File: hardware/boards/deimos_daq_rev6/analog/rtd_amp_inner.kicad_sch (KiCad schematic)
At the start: 22 parts, among them IC4001 INA826AIDR, IC4002 TLV333IDBVR, IC4003 TLV333IDBVR, U4001 NTJD4001NT1G

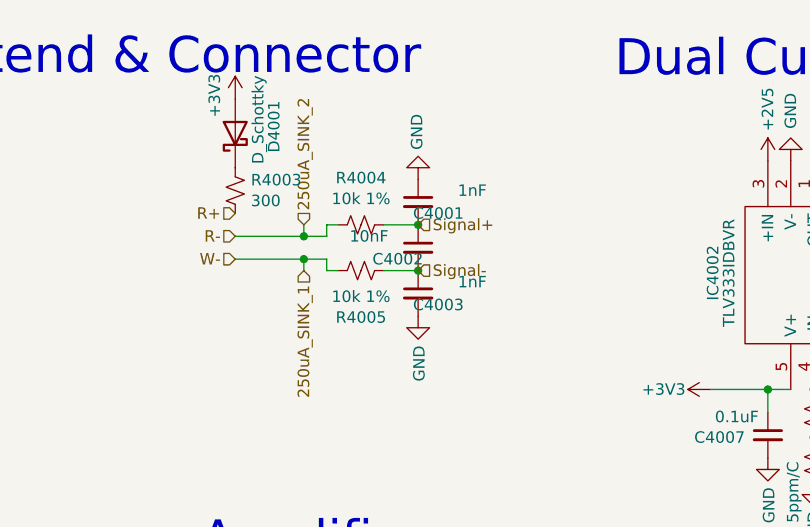
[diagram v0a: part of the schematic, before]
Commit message: move ovp diodes behind filter amps. wip to implement 5V LDO.
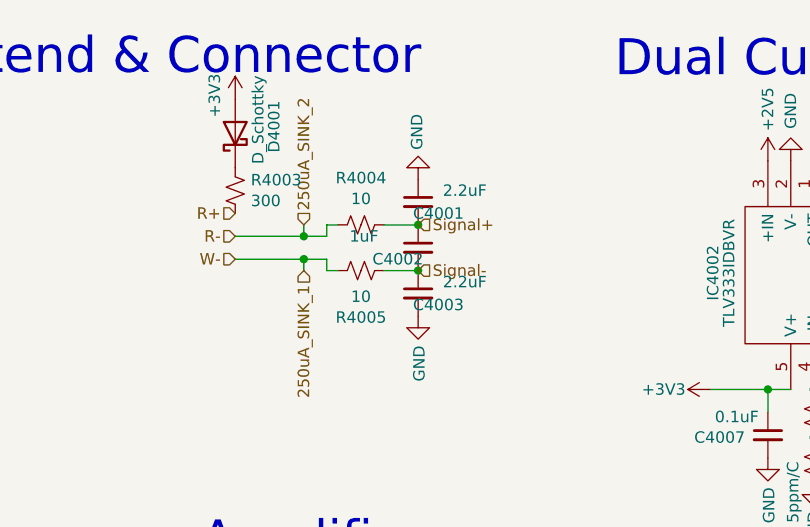
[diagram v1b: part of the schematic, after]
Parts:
- C4001, C4003: value 1nF -> 2.2uF
- C4002: value 10nF -> 1uF
- R4004, R4005: value 10k 1% -> 10
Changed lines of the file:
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@@
 			)
 		)
-		(property "Value" "10k 1%"
+		(property "Value" "10"
 			(at 121.92 65.4304 90)
 			(effects
@@
 			)
 		)
-		(property "Value" "1nF"
+		(property "Value" "2.2uF"
 			(at 135.89 64.516 0)
 			(effects
@@
 			)
 		)
-		(property "Value" "10nF"
+		(property "Value" "1uF"
 			(at 120.65 69.596 0)
 			(effects
@@
 			)
 		)
-		(property "Value" "10k 1%"
+		(property "Value" "10"
 			(at 121.92 76.3016 90)
 			(effects
@@
 			)
 		)
-		(property "Value" "1nF"
+		(property "Value" "2.2uF"
 			(at 135.89 74.676 0)
 			(effects

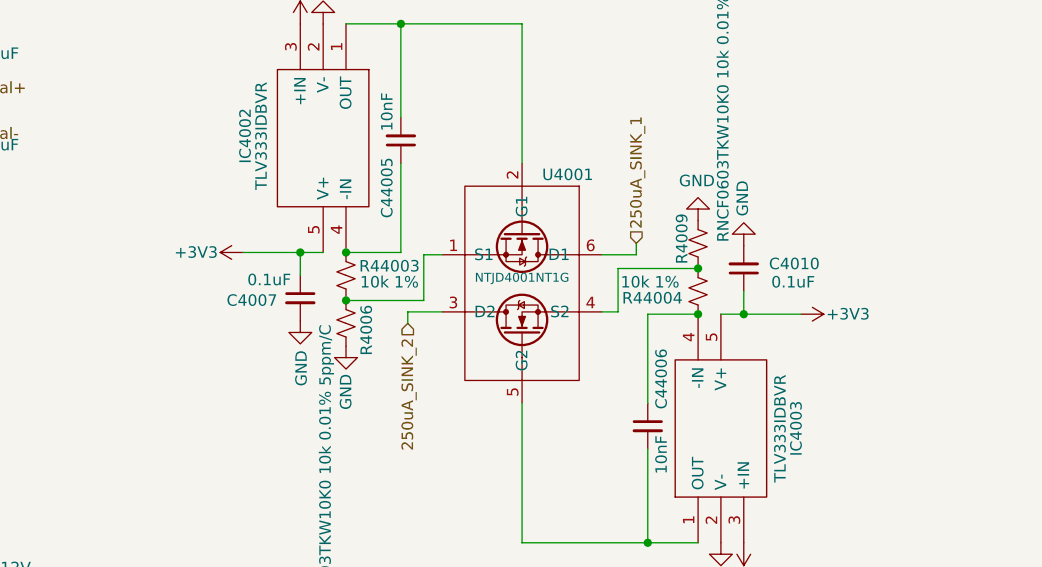
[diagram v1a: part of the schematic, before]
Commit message: run rtd amp current sinks on 5V supply
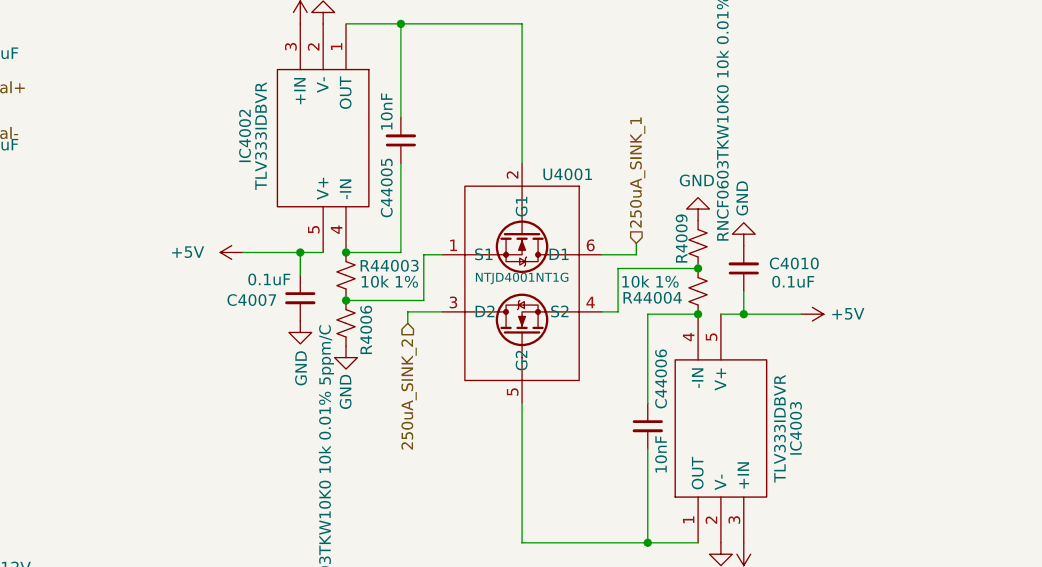
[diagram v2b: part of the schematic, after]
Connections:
- net +3V3: no longer C4007.1, C4010.1, IC4002.5 (V+), IC4003.5 (V+)
- new net +5V: C4007.1, C4010.1, IC4002.5 (V+), IC4003.5 (V+)
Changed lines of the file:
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@@
-	)
-	(symbol
-		(lib_id "power:+3V3")
-		(at 222.758 93.472 270)
-		(unit 1)
-		(exclude_from_sim no)
-		(in_bom yes)
-		(on_board yes)
-		(dnp no)
-		(property "Reference" "#PWR126"
-			(at 218.948 93.472 0)
-			(effects
-				(font
-					(size 1.27 1.27)
-				)
-				(hide yes)
-			)
-		)
-		(property "Value" "+3V3"
-			(at 225.552 93.472 90)
-			(effects
-				(font
-					(size 1.27 1.27)
-				)
-				(justify left)
-			)
-		)
-		(property "Footprint" ""
-			(at 222.758 93.472 0)
-			(effects
-				(font
-					(size 1.27 1.27)
-				)
-				(hide yes)
-			)
-		)
-		(property "Datasheet" ""
-			(at 222.758 93.472 0)
-			(effects
-				(font
-					(size 1.27 1.27)
-				)
-				(hide yes)
-			)
-		)
-		(property "Description" "Power symbol creates a global label with name \"+3V3\""
-			(at 222.758 93.472 0)
-			(effects
-				(font
-					(size 1.27 1.27)
-				)
-				(hide yes)
-			)
-		)
-		(pin "1"
-		)
-		(instances
-			(project "analog_i"
-				(path "/5a60c4b1-b6cb-416e-8883-8291fa089b87/c2baf18d-2b19-4edb-98b3-535275ee271f/a9caaa1d-d23d-426e-af7e-b0ee1cb64b05"
-					(reference "#PWR126")
-					(unit 1)
-				)
-				(path "/5a60c4b1-b6cb-416e-8883-8291fa089b87/c2baf18d-2b19-4edb-98b3-535275ee271f/19141585-7846-417a-91df-f61215fe3233/76bdcc3c-aeb3-45bb-bfec-f68418164bd8"
-					(reference "#PWR174")
-					(unit 1)
-				)
-				(path "/5a60c4b1-b6cb-416e-8883-8291fa089b87/c2baf18d-2b19-4edb-98b3-535275ee271f/1fbd3e63-3701-4f31-b722-16e65c25cea8/76bdcc3c-aeb3-45bb-bfec-f68418164bd8"
-					(reference "#PWR182")
-					(unit 1)
-				)
-				(path "/5a60c4b1-b6cb-416e-8883-8291fa089b87/c2baf18d-2b19-4edb-98b3-535275ee271f/fb5bb440-61c9-4bd3-9ab6-a463ad90c8bb/76bdcc3c-aeb3-45bb-bfec-f68418164bd8"
-					(reference "#PWR135")
-					(unit 1)
-				)
-			)
-			(project "analog_frontend_panel"
-				(path "/c241d083-1323-4b4a-a540-956d0afb7b72/a9caaa1d-d23d-426e-af7e-b0ee1cb64b05"
-					(reference "#PWR45003")
-					(unit 1)
-				)
-				(path "/c241d083-1323-4b4a-a540-956d0afb7b72/19141585-7846-417a-91df-f61215fe3233/76bdcc3c-aeb3-45bb-bfec-f68418164bd8"
-					(reference "#PWR46003")
-					(unit 1)
-				)
-				(path "/c241d083-1323-4b4a-a540-956d0afb7b72/1fbd3e63-3701-4f31-b722-16e65c25cea8/76bdcc3c-aeb3-45bb-bfec-f68418164bd8"
-					(reference "#PWR47003")
-					(unit 1)
-				)
-				(path "/c241d083-1323-4b4a-a540-956d0afb7b72/fb5bb440-61c9-4bd3-9ab6-a463ad90c8bb/76bdcc3c-aeb3-45bb-bfec-f68418164bd8"
-					(reference "#PWR44003")
-					(unit 1)
-				)
-			)
-		)
 	)
 	(symbol
@@
 	)
 	(symbol
-		(lib_id "power:+3V3")
+		(lib_id "power:+5V")
 		(at 160.782 86.614 90)
 		(unit 1)
@@
 		(on_board yes)
 		(dnp no)
-		(property "Reference" "#PWR125"
+		(fields_autoplaced yes)
+		(property "Reference" "#PWR47006"
 			(at 164.592 86.614 0)
 			(effects
@@
 			)
 		)
-		(property "Value" "+3V3"
-			(at 157.988 86.614 90)
+		(property "Value" "+5V"
+			(at 156.464 86.6139 90)
 			(effects
 				(font
@@
 			)
 		)
-		(property "Description" "Power symbol creates a global label with name \"+3V3\""
+		(property "Description" "Power symbol creates a global label with name \"+5V\""
 			(at 160.782 86.614 0)
 			(effects
@@
 		)
 		(instances
-			(project "analog_i"
-				(path "/5a60c4b1-b6cb-416e-8883-8291fa089b87/c2baf18d-2b19-4edb-98b3-535275ee271f/a9caaa1d-d23d-426e-af7e-b0ee1cb64b05"
-					(reference "#PWR125")
-					(unit 1)
-				)
-				(path "/5a60c4b1-b6cb-416e-8883-8291fa089b87/c2baf18d-2b19-4edb-98b3-535275ee271f/19141585-7846-417a-91df-f61215fe3233/76bdcc3c-aeb3-45bb-bfec-f68418164bd8"
-					(reference "#PWR173")
-					(unit 1)
-				)
-				(path "/5a60c4b1-b6cb-416e-8883-8291fa089b87/c2baf18d-2b19-4edb-98b3-535275ee271f/1fbd3e63-3701-4f31-b722-16e65c25cea8/76bdcc3c-aeb3-45bb-bfec-f68418164bd8"
-					(reference "#PWR181")
-					(unit 1)
-				)
-				(path "/5a60c4b1-b6cb-416e-8883-8291fa089b87/c2baf18d-2b19-4edb-98b3-535275ee271f/fb5bb440-61c9-4bd3-9ab6-a463ad90c8bb/76bdcc3c-aeb3-45bb-bfec-f68418164bd8"
-					(reference "#PWR134")
-					(unit 1)
-				)
-			)
-			(project "analog_frontend_panel"
+			(project ""
 				(path "/c241d083-1323-4b4a-a540-956d0afb7b72/a9caaa1d-d23d-426e-af7e-b0ee1cb64b05"
-					(reference "#PWR45002")
+					(reference "#PWR44005")
 					(unit 1)
 				)
 				(path "/c241d083-1323-4b4a-a540-956d0afb7b72/19141585-7846-417a-91df-f61215fe3233/76bdcc3c-aeb3-45bb-bfec-f68418164bd8"
-					(reference "#PWR46002")
+					(reference "#PWR46006")
 					(unit 1)
 				)
 				(path "/c241d083-1323-4b4a-a540-956d0afb7b72/1fbd3e63-3701-4f31-b722-16e65c25cea8/76bdcc3c-aeb3-45bb-bfec-f68418164bd8"
-					(reference "#PWR47002")
+					(reference "#PWR47006")
 					(unit 1)
 				)
 				(path "/c241d083-1323-4b4a-a540-956d0afb7b72/fb5bb440-61c9-4bd3-9ab6-a463ad90c8bb/76bdcc3c-aeb3-45bb-bfec-f68418164bd8"
-					(reference "#PWR44002")
+					(reference "#PWR45005")
 					(unit 1)
 				)
@@
 					(unit 1)
 				)
+			)
+		)
+	)
+	(symbol
+		(lib_id "power:+5V")
+		(at 222.758 93.472 270)
+		(unit 1)
+		(exclude_from_sim no)
+		(in_bom yes)
+		(on_board yes)
+		(dnp no)
+		(fields_autoplaced yes)
+		(property "Reference" "#PWR44002"
+			(at 218.948 93.472 0)
+			(effects
+				(font
+					(size 1.27 1.27)
+				)
+				(hide yes)
+			)
+		)
+		(property "Value" "+5V"
+			(at 226.06 93.4719 90)
+			(effects
+				(font
+					(size 1.27 1.27)
+				)
+				(justify left)
+			)
+		)
+		(property "Footprint" ""
+			(at 222.758 93.472 0)
+			(effects
+				(font
+					(size 1.27 1.27)
+				)
+				(hide yes)
+			)
+		)
+		(property "Datasheet" ""
+			(at 222.758 93.472 0)
+			(effects
+				(font
+					(size 1.27 1.27)
+				)
+				(hide yes)
+			)
+		)
+		(property "Description" "Power symbol creates a global label with name \"+5V\""
+			(at 222.758 93.472 0)
+			(effects
+				(font
+					(size 1.27 1.27)
+				)
+				(hide yes)
+			)
+		)
+		(pin "1"
+		)
+		(instances
+			(project "analog_frontend_panel"
+				(path "/c241d083-1323-4b4a-a540-956d0afb7b72/a9caaa1d-d23d-426e-af7e-b0ee1cb64b05"
+					(reference "#PWR44002")
+					(unit 1)
+				)
+				(path "/c241d083-1323-4b4a-a540-956d0afb7b72/19141585-7846-417a-91df-f61215fe3233/76bdcc3c-aeb3-45bb-bfec-f68418164bd8"
+					(reference "#PWR46002")
+					(unit 1)
+				)
+				(path "/c241d083-1323-4b4a-a540-956d0afb7b72/1fbd3e63-3701-4f31-b722-16e65c25cea8/76bdcc3c-aeb3-45bb-bfec-f68418164bd8"
+					(reference "#PWR47002")
+					(unit 1)
+				)
+				(path "/c241d083-1323-4b4a-a540-956d0afb7b72/fb5bb440-61c9-4bd3-9ab6-a463ad90c8bb/76bdcc3c-aeb3-45bb-bfec-f68418164bd8"
+					(reference "#PWR45002")
+					(unit 1)
+				)

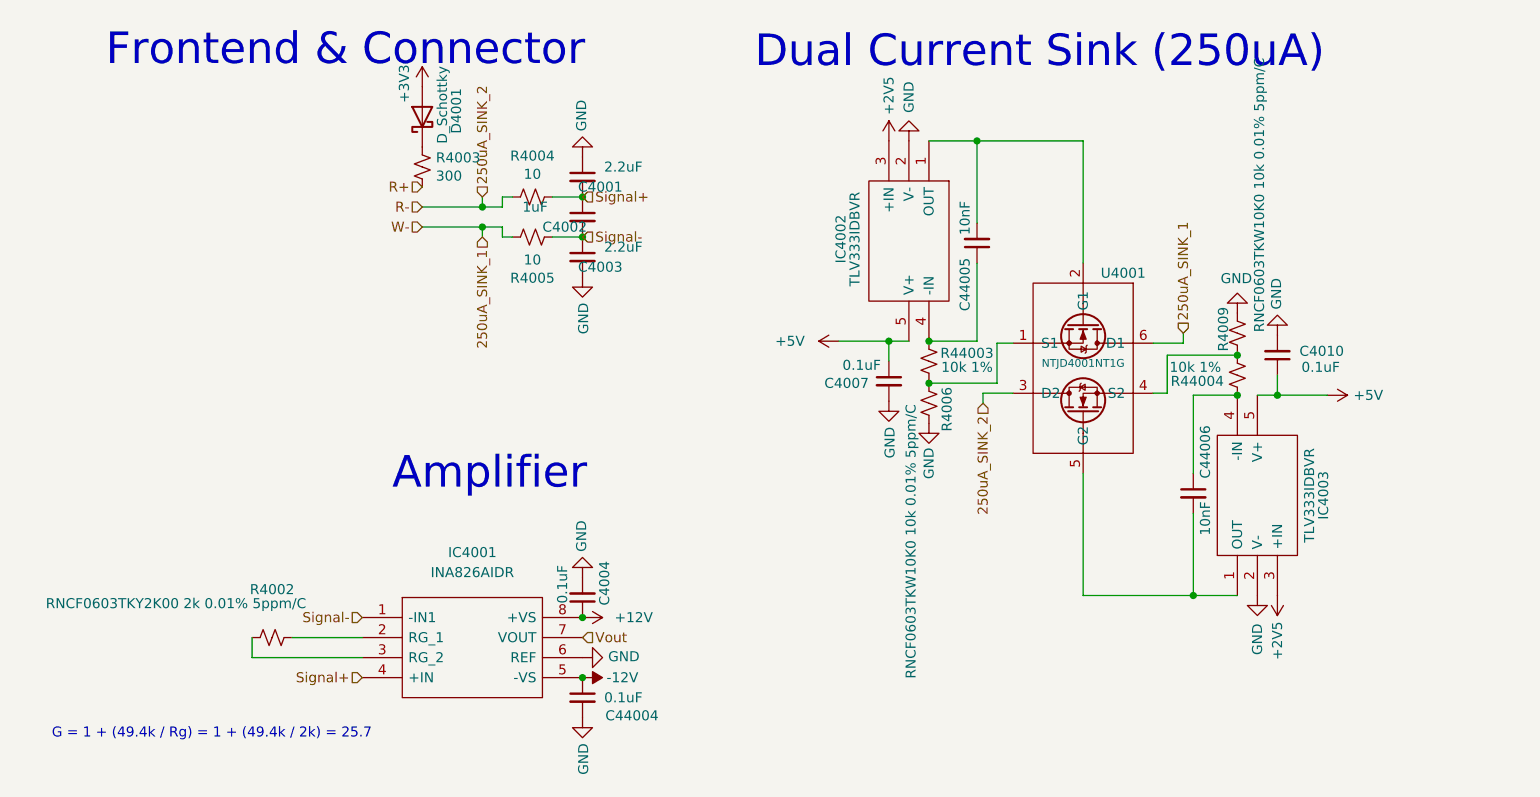
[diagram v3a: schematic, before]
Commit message: exclude testpoints from BOM
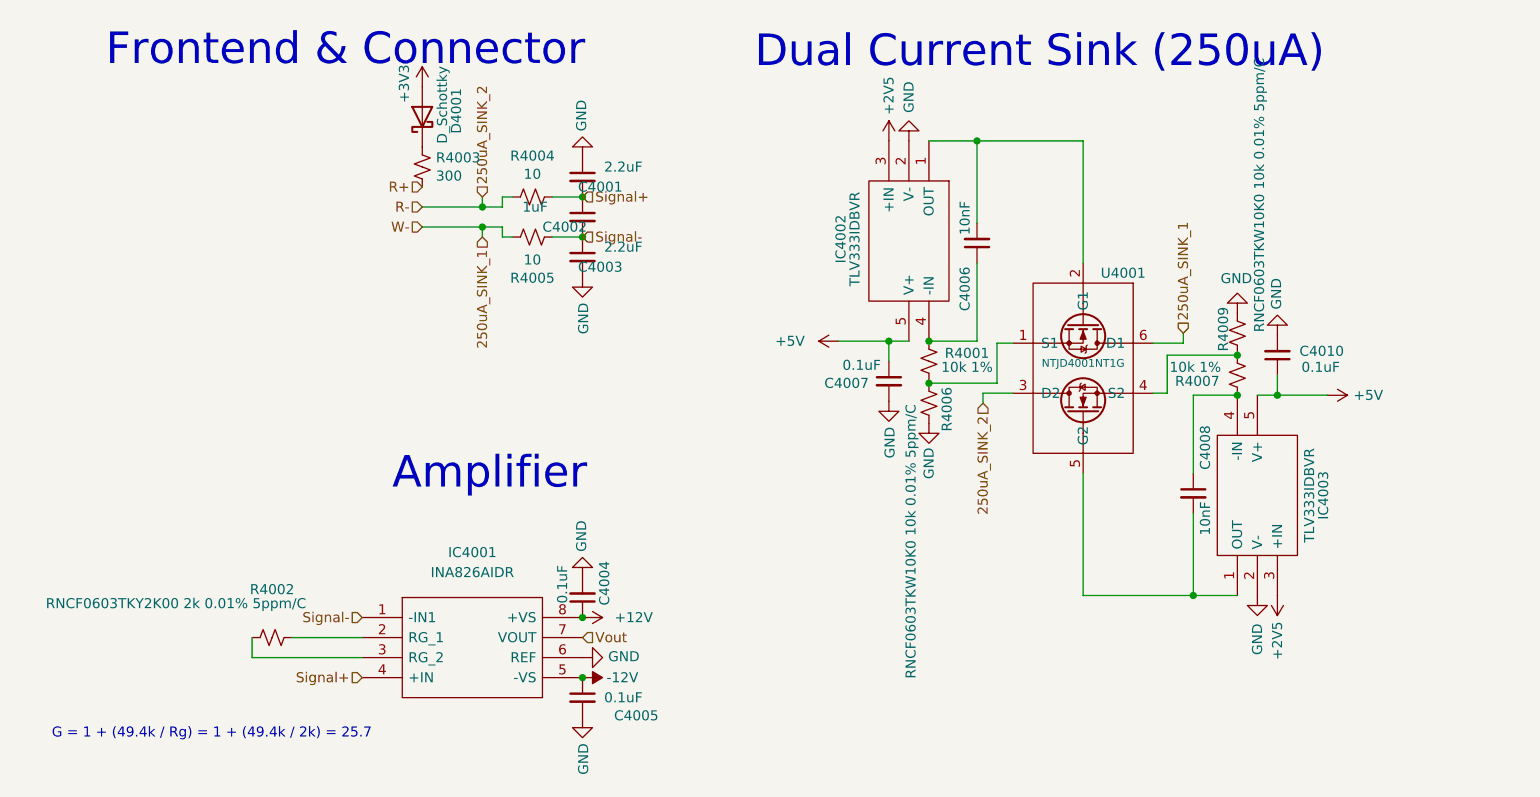
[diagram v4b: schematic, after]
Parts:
- renumbered C44004 to C4005, C44005 to C4006, C44006 to C4008, R44003 to R4001, R44004 to R4007
